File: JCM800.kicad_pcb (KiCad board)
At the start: 2 copper layers, 258.5 x 77.3 mm, 113 parts, among them U1 ECC83, U2 ECC83, U3 ECC83, U4 EL84, U5 EL84

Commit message: Fixed bias config
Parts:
- BIAS_U4, BIAS_U5: value B1M -> B5K
- R40, R41: value 47K -> 10K
- R42: value 47K -> 2K2
- moved GND2 150.6 mm to (76.7, 125.9)
- moved D5 0.41 mm to (175.3, 56.8)
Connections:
- D5 pad 1: /FIL -> /Tin2
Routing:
- net /Tin2: track 17.6 -> 96.5 mm, vias 0 -> 1
- net /FIL: track 260.0 -> 245.9 mm

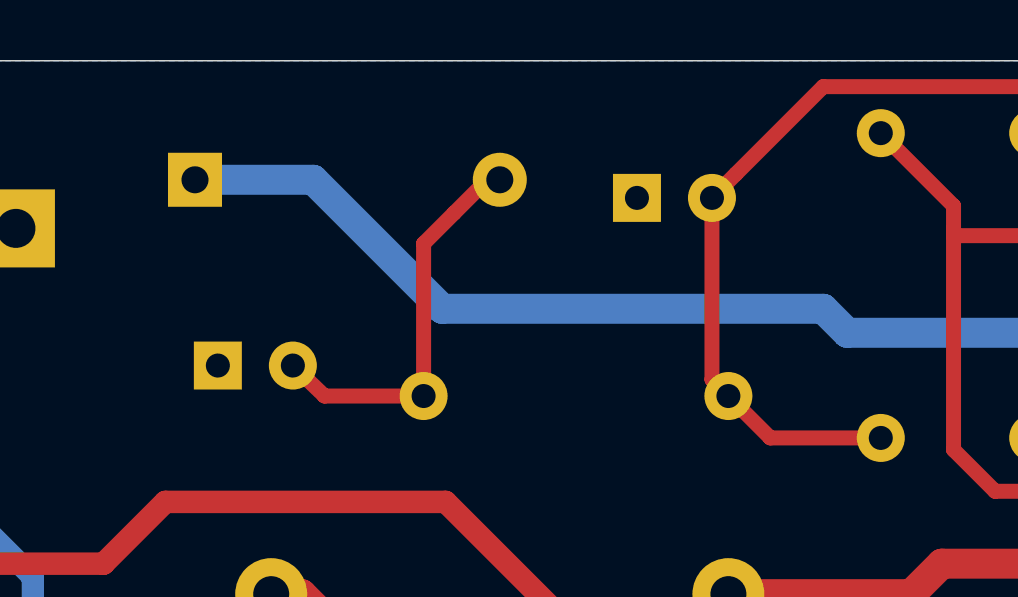
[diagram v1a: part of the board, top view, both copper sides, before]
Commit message: Fixed error in bias circuit
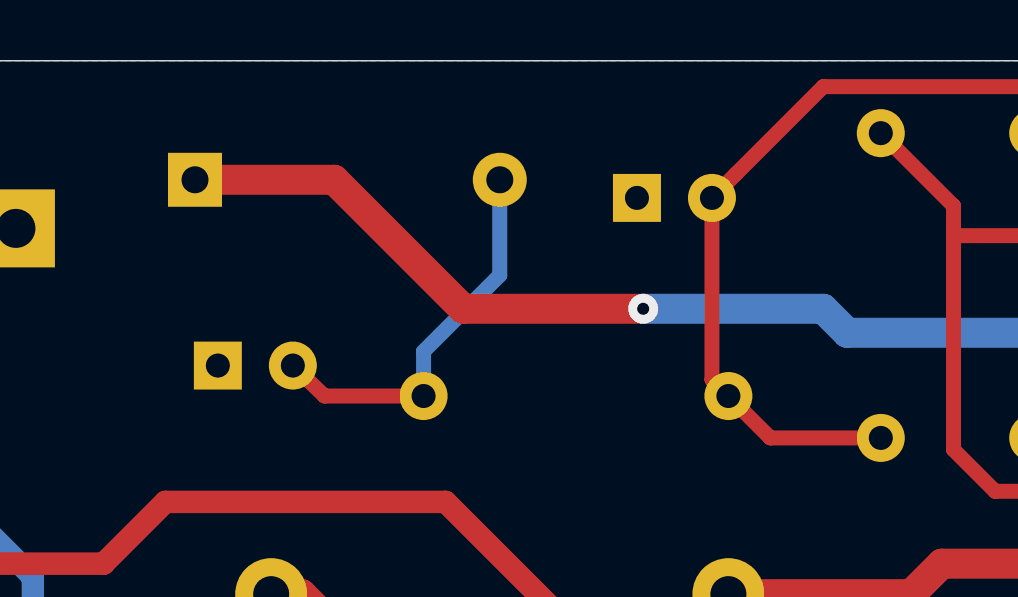
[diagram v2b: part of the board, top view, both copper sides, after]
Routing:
- net /Tin2: vias 1 -> 2
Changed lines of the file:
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@@
     (thickness 1.6)
     (drawings 24)
-    (tracks 639)
+    (tracks 641)
     (zones 0)
     (modules 113)
@@
   (segment (start 234.6 64.3) (end 228.1 64.3) (width 1) (layer F.Cu) (net 18))
   (segment (start 239.117 68.817) (end 234.6 64.3) (width 1) (layer F.Cu) (net 18))
-  (segment (start 179.2 56.8) (end 175.26 56.8) (width 1) (layer B.Cu) (net 18))
-  (segment (start 183.5 61.1) (end 179.2 56.8) (width 1) (layer B.Cu) (net 18))
-  (segment (start 196.2 61.1) (end 183.5 61.1) (width 1) (layer B.Cu) (net 18))
   (segment (start 197 61.9) (end 196.2 61.1) (width 1) (layer B.Cu) (net 18))
   (segment (start 210.3 61.9) (end 197 61.9) (width 1) (layer B.Cu) (net 18))
@@
   (segment (start 213.8 67.6) (end 213.8 65.4) (width 1) (layer B.Cu) (net 18))
   (segment (start 228.1 64.3) (end 225.2 64.3) (width 1) (layer B.Cu) (net 18))
+  (via (at 190.2 61.1) (size 1) (drill 0.4) (layers F.Cu B.Cu) (net 18))
+  (segment (start 196.2 61.1) (end 190.2 61.1) (width 1) (layer B.Cu) (net 18))
+  (segment (start 190.2 61.1) (end 184.2 61.1) (width 1) (layer F.Cu) (net 18))
+  (segment (start 179.9 56.8) (end 175.26 56.8) (width 1) (layer F.Cu) (net 18))
+  (segment (start 184.2 61.1) (end 179.9 56.8) (width 1) (layer F.Cu) (net 18))
   (via (at 133.223 127.381) (size 0.8) (drill 0.4) (layers F.Cu B.Cu) (net 19))
   (segment (start 196.87501 129.35499) (end 199 127.23) (width 0.5) (layer F.Cu) (net 19) (status 20))
@@
   (segment (start 219.707767 58.674) (end 217.043 61.338767) (width 0.5) (layer F.Cu) (net 56))
   (segment (start 209.677 64.008) (end 208.28 65.405) (width 0.5) (layer F.Cu) (net 56) (status 20))
-  (segment (start 185.42 56.388) (end 183.896 57.912) (width 0.5) (layer F.Cu) (net 57) (status 10))
-  (segment (start 182.88 58.928) (end 183.896 57.912) (width 0.5) (layer F.Cu) (net 57))
-  (segment (start 182.88 64.008) (end 182.88 58.928) (width 0.5) (layer F.Cu) (net 57) (status 10))
   (segment (start 179.578 64.008) (end 178.522 62.992) (width 0.5) (layer F.Cu) (net 57) (status 20))
   (segment (start 182.88 64.008) (end 179.578 64.008) (width 0.5) (layer F.Cu) (net 57) (status 10))
+  (segment (start 182.88 64.008) (end 182.88 62.52) (width 0.5) (layer B.Cu) (net 57))
+  (segment (start 185.42 59.98) (end 185.42 56.8) (width 0.5) (layer B.Cu) (net 57))
+  (segment (start 182.88 62.52) (end 185.42 59.98) (width 0.5) (layer B.Cu) (net 57))
   (segment (start 169.85 73.348949) (end 169.851666 73.347283) (width 0.75) (layer B.Cu) (net 58))
   (segment (start 169.85 75.145) (end 169.85 73.348949) (width 0.75) (layer B.Cu) (net 58) (status 10))

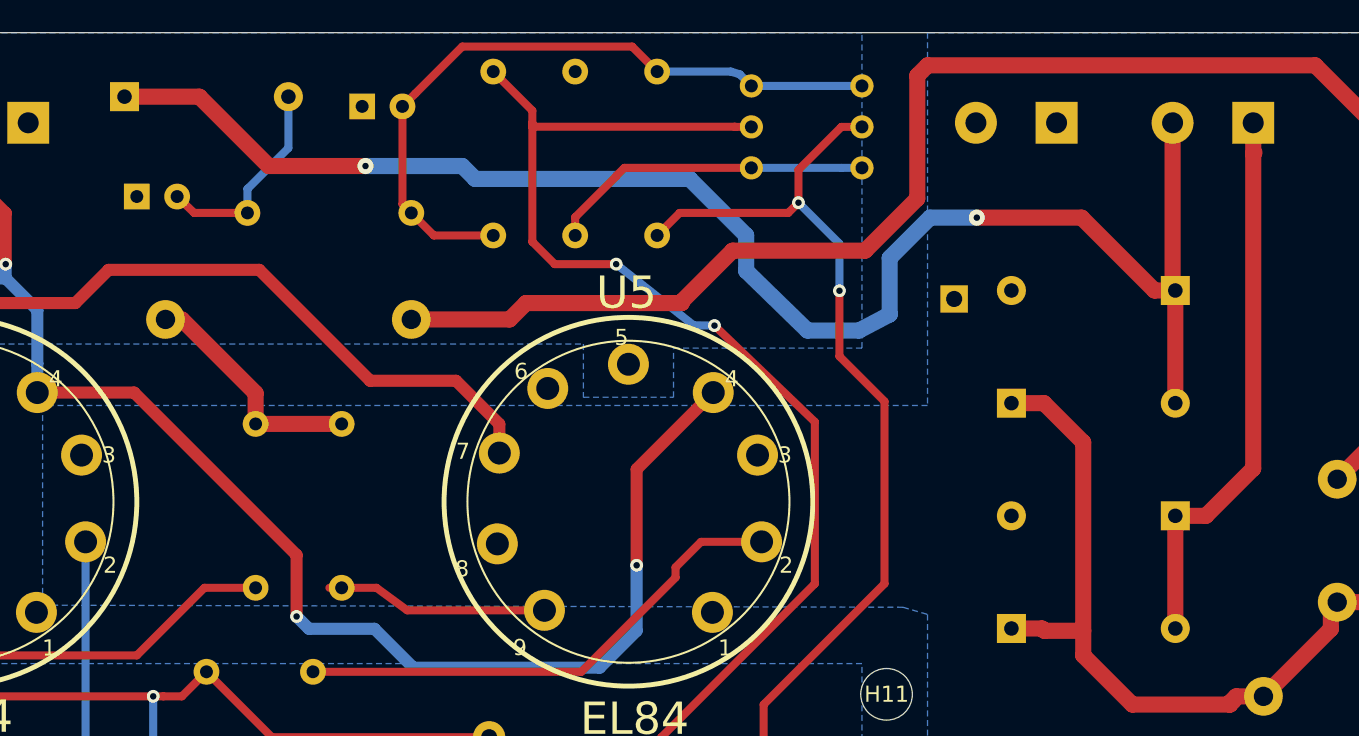
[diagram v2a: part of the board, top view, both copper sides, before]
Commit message: Taking the bias voltage from the HV transformer (requires transformer with central tap connected to GND)
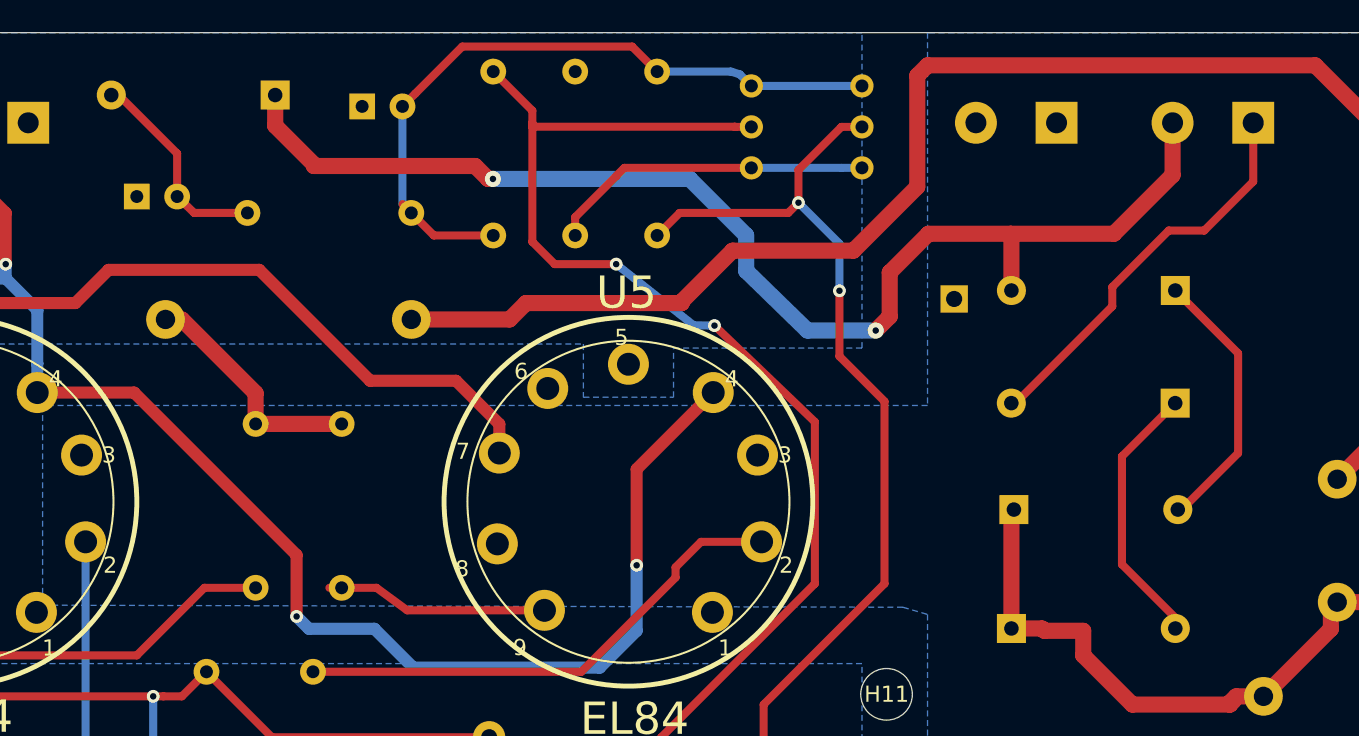
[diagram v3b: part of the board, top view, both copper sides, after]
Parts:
- moved D5 9.34 mm to (184.6, 56.7), turned to 180 degrees
- moved D2 6.99 mm to (240.4, 75.8)
- moved D3 6.60 mm to (230.4, 82.4)
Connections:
- D1 pad 2: /Tin1 -> Net-(D1-Pad2)
- D2 pad 1: /Tin1 -> Net-(D1-Pad2)
- D2 pad 2: GND -> /Tin1
- D3 pad 2: /Tin2 -> Net-(D3-Pad2)
- D4 pad 1: /Tin2 -> Net-(D3-Pad2)
- D4 pad 2: GND -> /Tin2
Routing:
- net /Tin2: track 96.5 -> 76.5 mm
- net Net-(D3-Pad2): track 0.00 -> 16.9 mm
- net Net-(D1-Pad2): track 0.00 -> 16.7 mm
- net /A: track 88.3 -> 78.6 mm
- net /Tin1: track 34.8 -> 25.3 mm

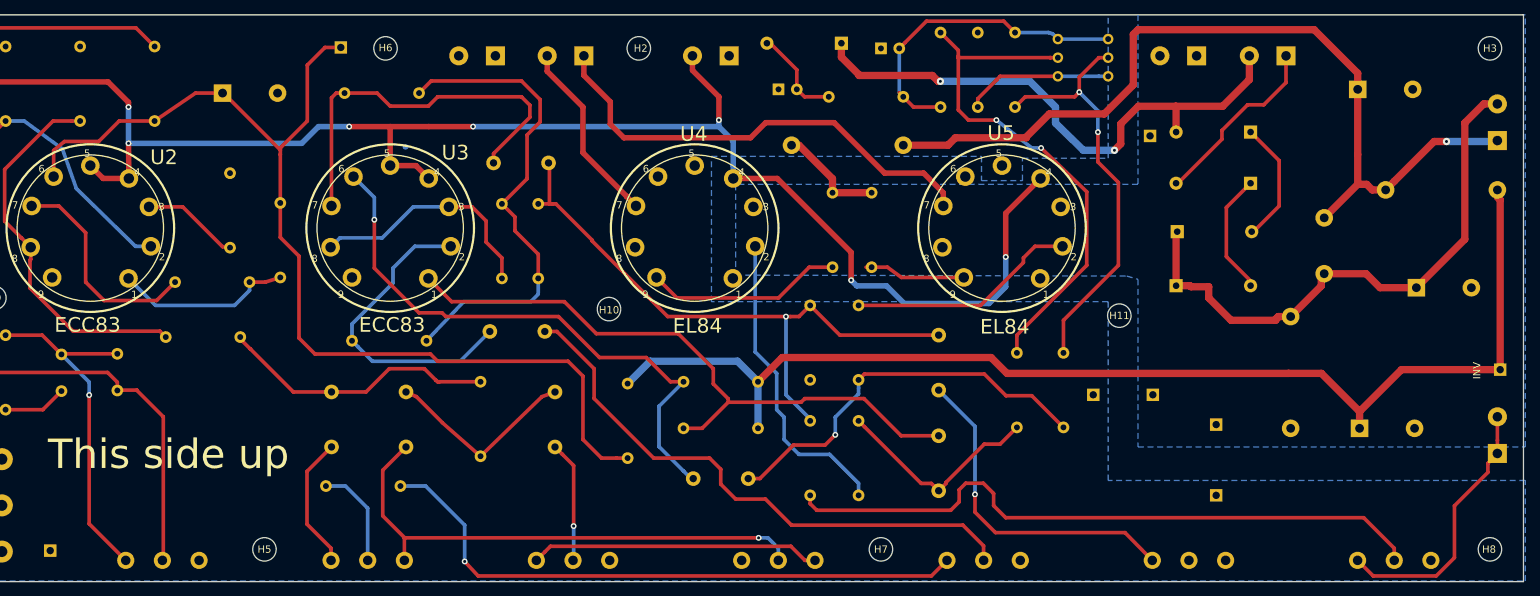
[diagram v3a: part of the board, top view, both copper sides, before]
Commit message: Fixed bias circuit
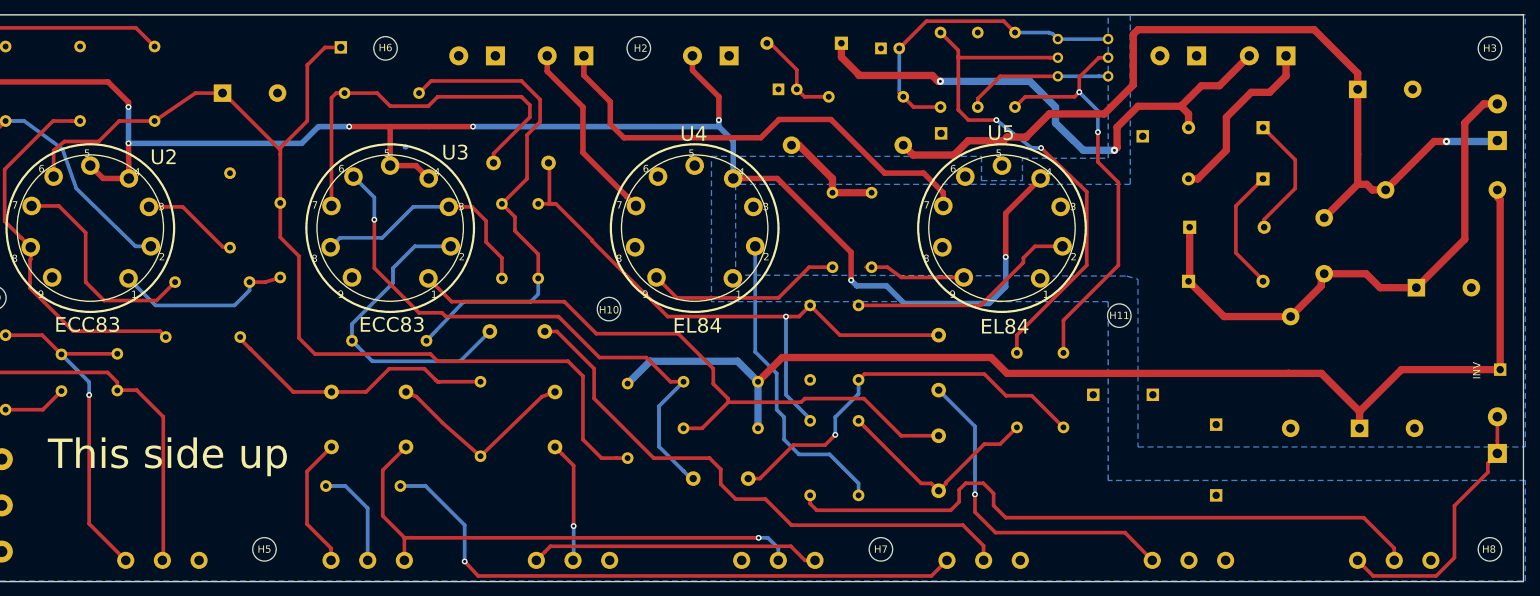
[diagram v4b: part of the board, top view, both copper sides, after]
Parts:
- moved GND2 134.2 mm to (198.2, 69.0)
- moved D1 1.80 mm to (231.9, 89.2)
- moved D3 1.80 mm to (232.1, 81.8)
- moved D2 1.80 mm to (242.1, 75.2)
- moved D4 1.80 mm to (242.1, 68.2)
- moved GND1 1.00 mm to (225.7, 69.4)
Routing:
- net /A: track 78.6 -> 75.4 mm
- net /Tin2: track 76.5 -> 74.4 mm
- net /B: track 118.8 -> 120.0 mm
- net /Tin1: track 25.3 -> 24.7 mm

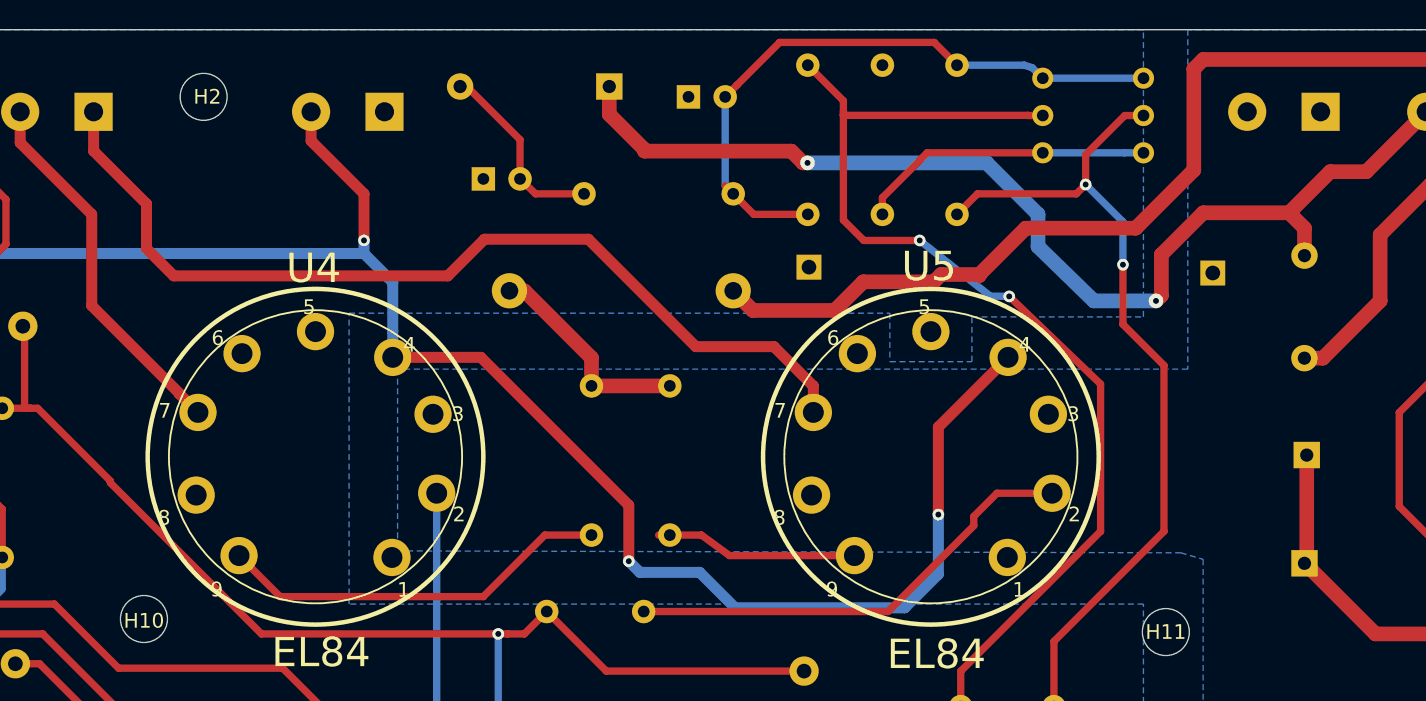
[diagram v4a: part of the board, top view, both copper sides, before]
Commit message: Fixed bias circuit
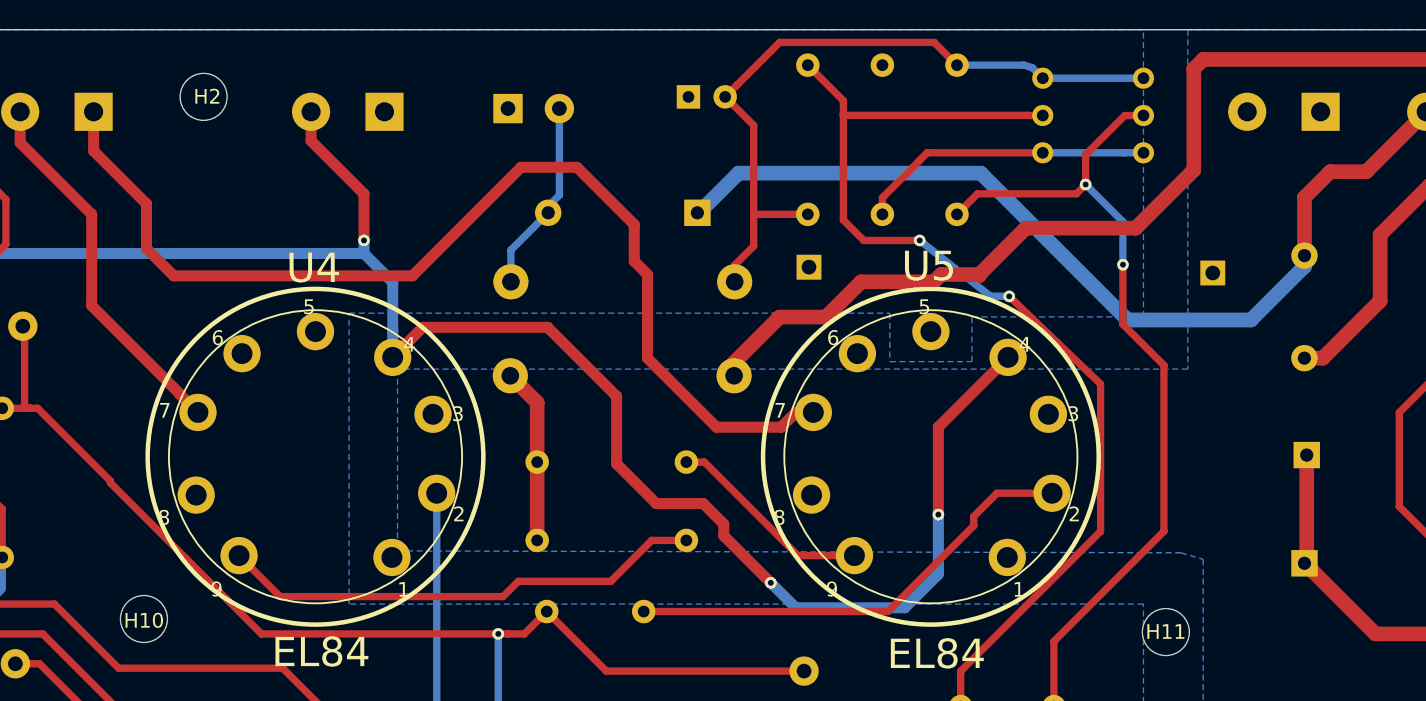
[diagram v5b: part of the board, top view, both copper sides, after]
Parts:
- C23: value 68u -> 10uF/400V; footprint Capacitor_THT:CP_Radial_D6.3mm_P2.50mm -> Capacitor_THT:CP_Radial_D10.0mm_P3.50mm
- C24: value 68u -> 68uF/35V
- R39: value 47K -> 82K/3W; footprint Resistor_THT:R_Axial_DIN0207_L6.3mm_D2.5mm_P10.16mm_Horizontal -> Resistor_THT:R_Axial_DIN0414_L11.9mm_D4.5mm_P15.24mm_Horizontal
- moved D5 10.5 mm to (190.6, 65.3)
- moved R35 10.4 mm to (179.7, 82.3), turned to 0 degrees
- moved R39 7.79 mm to (177.9, 70.0)
- moved R34 6.47 mm to (189.8, 87.6), turned to 180 degrees
- moved R38 5.79 mm to (193.1, 76.4)
- moved C23 5.08 mm to (177.7, 58.2)
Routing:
- net /Tin2: track 74.4 -> 63.6 mm, vias 2 -> 0
- net /OUT2: track 64.0 -> 72.6 mm
- net Net-(R34-Pad1): track 26.9 -> 33.2 mm
- net Net-(BIAS_U4-Pad1): track 43.5 -> 48.6 mm
- net Net-(R34-Pad2): track 14.7 -> 12.0 mm
- net /FIL: track 245.9 -> 248.5 mm
- net /B: track 120.0 -> 121.7 mm
